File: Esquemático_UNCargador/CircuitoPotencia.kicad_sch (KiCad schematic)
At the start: 0 parts

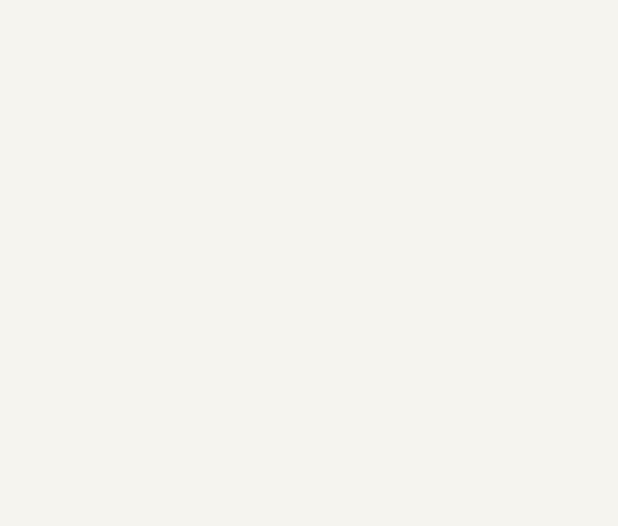
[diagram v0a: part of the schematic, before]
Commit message: Se modifica esquema del micro y se agrega página de sensores
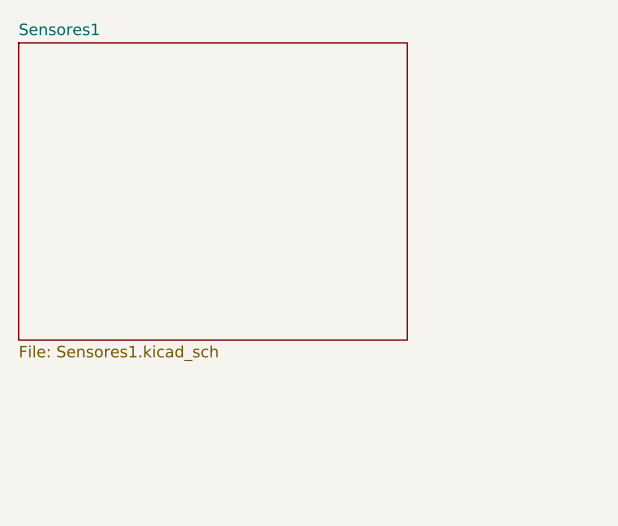
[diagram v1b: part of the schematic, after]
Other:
- added sheet Sensores1 (Sensores1.kicad_sch)
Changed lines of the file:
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@@
+    )
+  )
+  (sheet (at 55.88 40.64) (size 43.18 33.02) (fields_autoplaced)
+    (stroke (width 0.1524) (type solid))
+    (fill (color 0 0 0 0.0000))
+    (property "Sheetname" "Sensores1" (at 55.88 39.9284 0)
+      (effects (font (size 1.27 1.27)) (justify left bottom))
+    )
+    (property "Sheetfile" "Sensores1.kicad_sch" (at 55.88 74.2446 0)
+      (effects (font (size 1.27 1.27)) (justify left top))
+    )
+    (instances
+      (project "CircuitoPotencia"
+        (path "/f64e4c48-29c2-4644-b6e3-d55b9152fc29" (page "5"))
+      )
     )
   )

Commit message: Pinout sensores
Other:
- sheet Microcontrolador ports: added FALLA, GFCI_TEST, NTC_Analog, RX_01, TX_01; removed none
- sheet Sensores1 ports: added FALLA, GFCI_TEST, NTC_Analog, RX_01, TX_01; removed none
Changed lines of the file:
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@@
 (kicad_sch (version 20230121) (generator eeschema)
   (paper "A4")
+  (wire (pts (xy 89.3064 73.66) (xy 89.3064 118.11))
+    (stroke (width 0) (type default))
+  )
+  (wire (pts (xy 67.564 73.66) (xy 67.564 118.11))
+    (stroke (width 0) (type default))
+  )
+  (wire (pts (xy 79.9592 73.66) (xy 79.9592 118.11))
+    (stroke (width 0) (type default))
+  )
+  (wire (pts (xy 83.7692 73.66) (xy 83.7692 118.11))
+    (stroke (width 0) (type default))
+  )
   (wire (pts (xy 96.52 134.62) (xy 133.35 134.62))
+    (stroke (width 0) (type default))
+  )
+  (wire (pts (xy 83.7692 73.66) (xy 83.7184 73.66))
+    (stroke (width 0) (type default))
+  )
+  (wire (pts (xy 73.8124 73.66) (xy 73.8124 118.11))
+    (stroke (width 0) (type default))
+  )
+  (wire (pts (xy 79.9592 118.11) (xy 79.9084 118.11))
     (stroke (width 0) (type default))
   )
@@
     )
     (pin "pilot_PWM" output (at 96.52 134.62 0)
+      (effects (font (size 1.27 1.27)) (justify right))
+    )
+    (pin "GFCI_TEST" input (at 89.3064 118.11 90)
+      (effects (font (size 1.27 1.27)) (justify right))
+    )
+    (pin "FALLA" input (at 67.564 118.11 90)
+      (effects (font (size 1.27 1.27)) (justify right))
+    )
+    (pin "NTC_Analog" input (at 73.8124 118.11 90)
+      (effects (font (size 1.27 1.27)) (justify right))
+    )
+    (pin "RX_01" input (at 79.9084 118.11 90)
+      (effects (font (size 1.27 1.27)) (justify right))
+    )
+    (pin "TX_01" input (at 83.7692 118.11 90)
       (effects (font (size 1.27 1.27)) (justify right))
     )
@@
       (effects (font (size 1.27 1.27)) (justify left top))
     )
+    (pin "FALLA" input (at 67.564 73.66 270)
+      (effects (font (size 1.27 1.27)) (justify left))
+    )
+    (pin "RX_01" input (at 79.9592 73.66 270)
+      (effects (font (size 1.27 1.27)) (justify left))
+    )
+    (pin "GFCI_TEST" input (at 89.3064 73.66 270)
+      (effects (font (size 1.27 1.27)) (justify left))
+    )
+    (pin "TX_01" input (at 83.7184 73.66 270)
+      (effects (font (size 1.27 1.27)) (justify left))
+    )
+    (pin "NTC_Analog" input (at 73.8124 73.66 270)
+      (effects (font (size 1.27 1.27)) (justify left))
+    )
     (instances

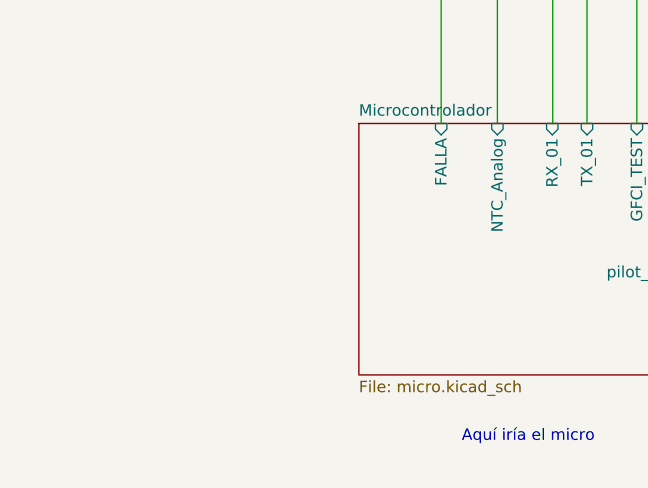
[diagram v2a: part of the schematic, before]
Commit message: Avances en Huellas
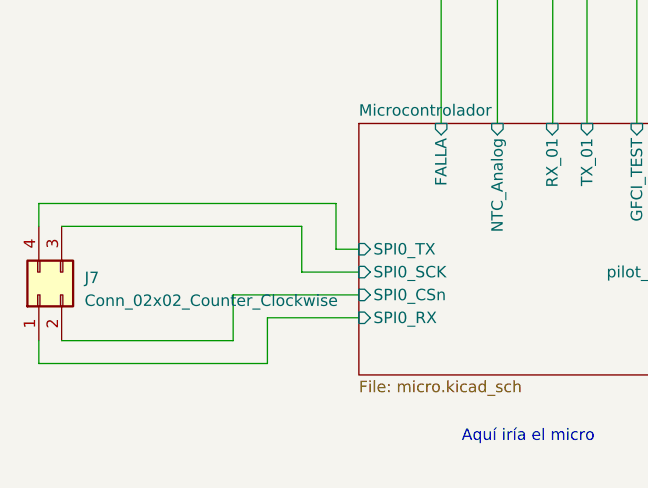
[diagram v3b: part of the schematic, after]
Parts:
- added J7: Conn_02x02_Counter_Clockwise, Connector_PinHeader_2.54mm:PinHeader_2x02_P2.54mm_Vertical, symbol Connector_Generic:Conn_02x02_Counter_Clockwise
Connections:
- new net Microcontrolador/SPI0_CSn: J7.2 (Pin_2)
- new net Microcontrolador/SPI0_RX: J7.1 (Pin_1)
- new net Microcontrolador/SPI0_SCK: J7.3 (Pin_3)
- new net Microcontrolador/SPI0_TX: J7.4 (Pin_4)
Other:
- sheet Microcontrolador ports: added SPI0_CSn, SPI0_RX, SPI0_SCK, SPI0_TX; removed none
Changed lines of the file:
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@@
 (kicad_sch (version 20230121) (generator eeschema)
   (paper "A4")
+  (wire (pts (xy 48.26 139.7) (xy 58.42 139.7))
+    (stroke (width 0) (type default))
+  )
+  (wire (pts (xy 52.07 134.62) (xy 52.07 129.54))
+    (stroke (width 0) (type default))
+  )
+  (wire (pts (xy 44.45 142.24) (xy 44.45 137.16))
+    (stroke (width 0) (type default))
+  )
   (wire (pts (xy 89.3064 73.66) (xy 89.3064 118.11))
+    (stroke (width 0) (type default))
+  )
+  (wire (pts (xy 58.42 134.62) (xy 52.07 134.62))
+    (stroke (width 0) (type default))
+  )
+  (wire (pts (xy 22.86 129.54) (xy 22.86 127))
+    (stroke (width 0) (type default))
+  )
+  (wire (pts (xy 55.88 127) (xy 55.88 132.08))
     (stroke (width 0) (type default))
   )
@@
     (stroke (width 0) (type default))
   )
+  (wire (pts (xy 52.07 129.54) (xy 25.4 129.54))
+    (stroke (width 0) (type default))
+  )
+  (wire (pts (xy 22.86 142.24) (xy 22.86 144.78))
+    (stroke (width 0) (type default))
+  )
   (wire (pts (xy 96.52 134.62) (xy 133.35 134.62))
+    (stroke (width 0) (type default))
+  )
+  (wire (pts (xy 44.45 137.16) (xy 58.42 137.16))
+    (stroke (width 0) (type default))
+  )
+  (wire (pts (xy 25.4 142.24) (xy 44.45 142.24))
     (stroke (width 0) (type default))
   )
@@
   )
   (wire (pts (xy 79.9592 118.11) (xy 79.9084 118.11))
+    (stroke (width 0) (type default))
+  )
+  (wire (pts (xy 22.86 144.78) (xy 48.26 144.78))
+    (stroke (width 0) (type default))
+  )
+  (wire (pts (xy 55.88 132.08) (xy 58.42 132.08))
+    (stroke (width 0) (type default))
+  )
+  (wire (pts (xy 22.86 127) (xy 55.88 127))
+    (stroke (width 0) (type default))
+  )
+  (wire (pts (xy 48.26 144.78) (xy 48.26 139.7))
     (stroke (width 0) (type default))
   )
@@
     (at 142.24 82.55 0)
     (effects (font (size 1.27 1.27)) (justify left bottom))
+  )
+  (symbol (lib_id "Connector_Generic:Conn_02x02_Counter_Clockwise") (at 22.86 137.16 90) (unit 1)
+    (in_bom yes) (on_board yes) (dnp no) (fields_autoplaced)
+    (property "Reference" "J7" (at 27.94 135.255 90)
+      (effects (font (size 1.27 1.27)) (justify right))
+    )
+    (property "Value" "Conn_02x02_Counter_Clockwise" (at 27.94 137.795 90)
+      (effects (font (size 1.27 1.27)) (justify right))
+    )
+    (property "Footprint" "Connector_PinHeader_2.54mm:PinHeader_2x02_P2.54mm_Vertical" (at 22.86 137.16 0)
+      (effects (font (size 1.27 1.27)) hide)
+    )
+    (property "Datasheet" "~" (at 22.86 137.16 0)
+      (effects (font (size 1.27 1.27)) hide)
+    )
+    (pin "1")
+    (pin "2")
+    (pin "3")
+    (pin "4")
+    (instances
+      (project "CircuitoPotencia"
+        (path "/f64e4c48-29c2-4644-b6e3-d55b9152fc29"
+          (reference "J7") (unit 1)
+        )
+      )
+    )
   )
   (sheet (at 58.42 118.11) (size 38.1 27.94) (fields_autoplaced)
@@
       (effects (font (size 1.27 1.27)) (justify right))
     )
+    (pin "SPI0_TX" input (at 58.42 132.08 180)
+      (effects (font (size 1.27 1.27)) (justify left))
+    )
+    (pin "SPI0_SCK" input (at 58.42 134.62 180)
+      (effects (font (size 1.27 1.27)) (justify left))
+    )
+    (pin "SPI0_CSn" input (at 58.42 137.16 180)
+      (effects (font (size 1.27 1.27)) (justify left))
+    )
+    (pin "SPI0_RX" input (at 58.42 139.7 180)
+      (effects (font (size 1.27 1.27)) (justify left))
+    )
     (instances

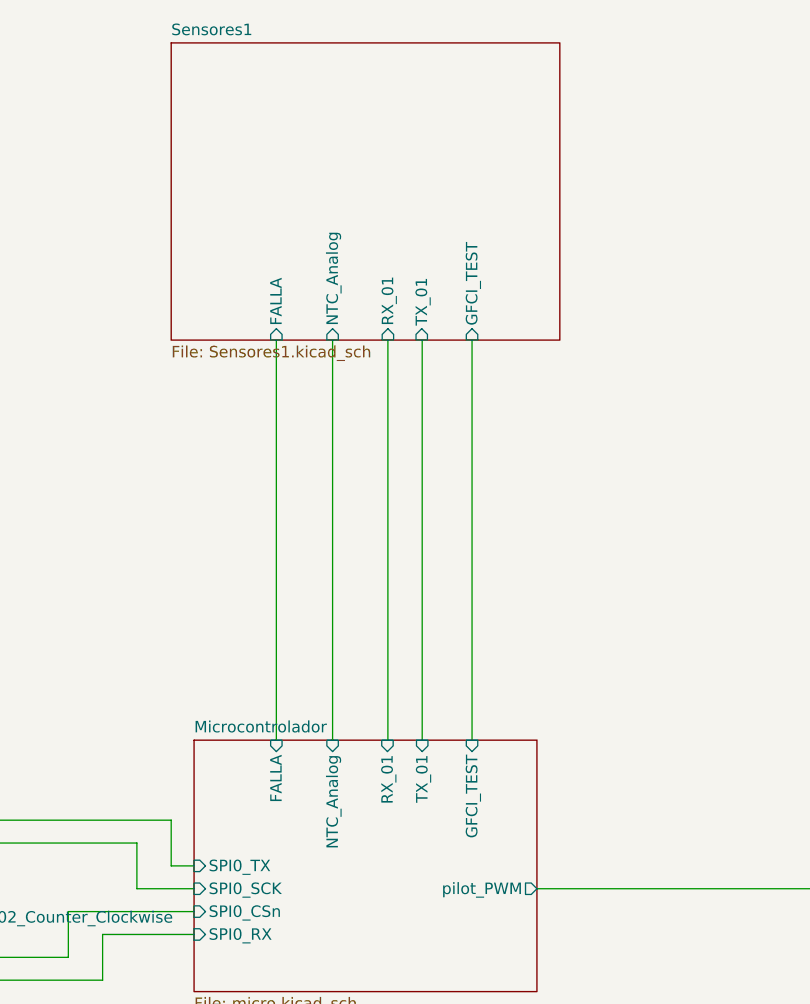
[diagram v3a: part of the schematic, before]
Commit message: Modificación de la huella del microcontrolador
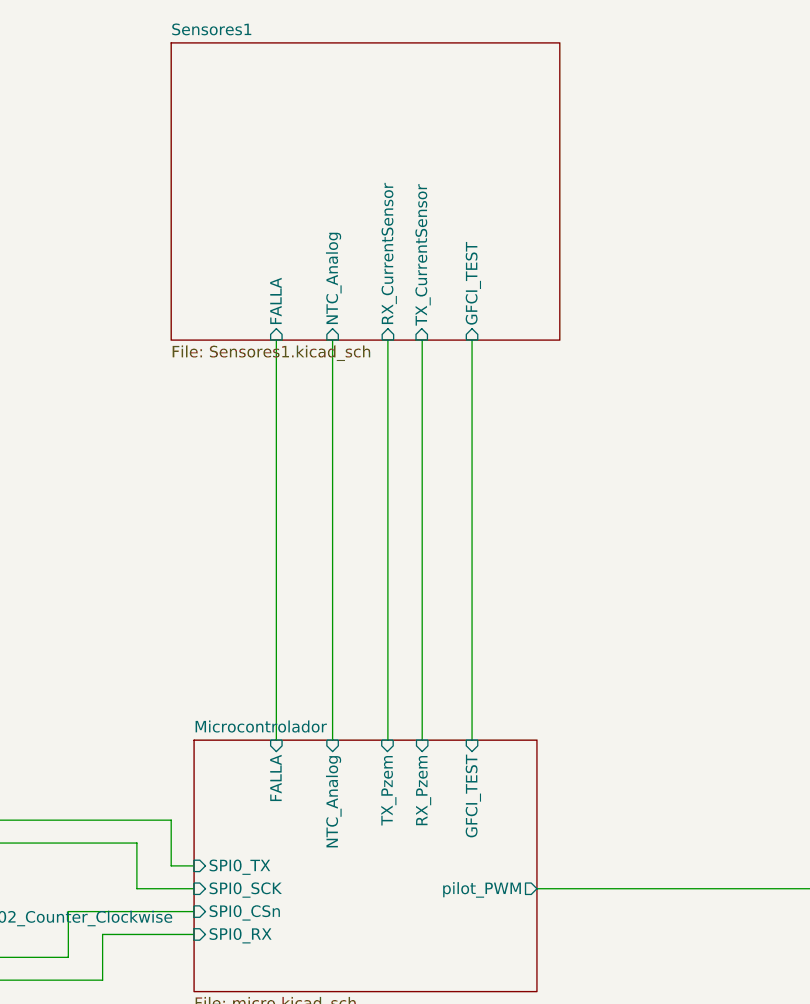
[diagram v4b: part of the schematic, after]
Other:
- sheet Microcontrolador ports: added RX_Pzem, TX_Pzem; removed RX_01, TX_01
- sheet Sensores1 ports: added RX_CurrentSensor, TX_CurrentSensor; removed RX_01, TX_01
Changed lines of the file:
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@@
       (effects (font (size 1.27 1.27)) (justify right))
     )
-    (pin "RX_01" input (at 79.9084 118.11 90)
+    (pin "TX_Pzem" input (at 79.9084 118.11 90)
       (effects (font (size 1.27 1.27)) (justify right))
     )
-    (pin "TX_01" input (at 83.7692 118.11 90)
+    (pin "RX_Pzem" input (at 83.7692 118.11 90)
       (effects (font (size 1.27 1.27)) (justify right))
     )
@@
       (effects (font (size 1.27 1.27)) (justify left))
     )
-    (pin "RX_01" input (at 79.9592 73.66 270)
+    (pin "RX_CurrentSensor" input (at 79.9592 73.66 270)
       (effects (font (size 1.27 1.27)) (justify left))
     )
@@
       (effects (font (size 1.27 1.27)) (justify left))
     )
-    (pin "TX_01" input (at 83.7184 73.66 270)
+    (pin "TX_CurrentSensor" input (at 83.7184 73.66 270)
       (effects (font (size 1.27 1.27)) (justify left))
     )

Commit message: Cambios de recomendaciones profesor
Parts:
- removed J7: Conn_02x02_Counter_Clockwise, Connector_PinHeader_2.54mm:PinHeader_2x02_P2.54mm_Vertical, symbol Connector_Generic:Conn_02x02_Counter_Clockwise
- added J2: InV, Connector_Molex:Molex_KK-254_AE-6410-02A_1x02_P2.54mm_Vertical, symbol Connector:Conn_01x02_Socket
- added J3: Conn_02x03_Counter_Clockwise, Connector_PinHeader_2.54mm:PinHeader_2x03_P2.54mm_Vertical, symbol Connector_Generic:Conn_02x03_Counter_Clockwise
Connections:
- net Microcontrolador/SPI0_CSn: now also J3.3 (Pin_3)
- net Microcontrolador/SPI0_RX: now also J3.2 (Pin_2)
- net Microcontrolador/SPI0_SCK: now also J3.4 (Pin_4)
- net Microcontrolador/SPI0_TX: now also J3.5 (Pin_5)
- new net GND: J3.1 (Pin_1)
- new net Potencia2.0/In110v: J2.1 (Pin_1)
- new net Potencia2.0/N: J2.2 (Pin_2)
- no-connect marks 0 -> 1
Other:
- sheet Potencia2.0 ports: added In110v, N; removed none
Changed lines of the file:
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@@
 (kicad_sch (version 20230121) (generator eeschema)
   (paper "A4")
+  (no_connect (at 20.32 129.54))
   (wire (pts (xy 48.26 139.7) (xy 58.42 139.7))
     (stroke (width 0) (type default))
@@
     (stroke (width 0) (type default))
   )
+  (wire (pts (xy 185.42 57.15) (xy 181.61 57.15))
+    (stroke (width 0) (type default))
+  )
   (wire (pts (xy 83.7692 73.66) (xy 83.7692 118.11))
     (stroke (width 0) (type default))
@@
     (stroke (width 0) (type default))
   )
+  (wire (pts (xy 189.23 55.88) (xy 185.42 55.88))
+    (stroke (width 0) (type default))
+  )
+  (wire (pts (xy 185.42 53.34) (xy 185.42 52.07))
+    (stroke (width 0) (type default))
+  )
   (wire (pts (xy 22.86 142.24) (xy 22.86 144.78))
     (stroke (width 0) (type default))
   )
+  (wire (pts (xy 189.23 53.34) (xy 185.42 53.34))
+    (stroke (width 0) (type default))
+  )
   (wire (pts (xy 96.52 134.62) (xy 133.35 134.62))
     (stroke (width 0) (type default))
@@
     (stroke (width 0) (type default))
   )
+  (wire (pts (xy 20.32 142.24) (xy 20.32 146.05))
+    (stroke (width 0) (type default))
+  )
   (wire (pts (xy 25.4 142.24) (xy 44.45 142.24))
     (stroke (width 0) (type default))
   )
   (wire (pts (xy 83.7692 73.66) (xy 83.7184 73.66))
+    (stroke (width 0) (type default))
+  )
+  (wire (pts (xy 185.42 52.07) (xy 181.61 52.07))
+    (stroke (width 0) (type default))
+  )
+  (wire (pts (xy 185.42 55.88) (xy 185.42 57.15))
     (stroke (width 0) (type default))
   )
@@
     (effects (font (size 1.27 1.27)) (justify left bottom))
   )
-  (symbol (lib_id "Connector_Generic:Conn_02x02_Counter_Clockwise") (at 22.86 137.16 90) (unit 1)
+  (symbol (lib_id "power:GND") (at 20.32 146.05 0) (unit 1)
     (in_bom yes) (on_board yes) (dnp no) (fields_autoplaced)
-    (property "Reference" "J7" (at 27.94 135.255 90)
-      (effects (font (size 1.27 1.27)) (justify right))
-    )
-    (property "Value" "Conn_02x02_Counter_Clockwise" (at 27.94 137.795 90)
-      (effects (font (size 1.27 1.27)) (justify right))
-    )
-    (property "Footprint" "Connector_PinHeader_2.54mm:PinHeader_2x02_P2.54mm_Vertical" (at 22.86 137.16 0)
+    (property "Reference" "#PWR011" (at 20.32 152.4 0)
+      (effects (font (size 1.27 1.27)) hide)
+    )
+    (property "Value" "GND" (at 20.32 151.13 0)
+      (effects (font (size 1.27 1.27)))
+    )
+    (property "Footprint" "" (at 20.32 146.05 0)
+      (effects (font (size 1.27 1.27)) hide)
+    )
+    (property "Datasheet" "" (at 20.32 146.05 0)
+      (effects (font (size 1.27 1.27)) hide)
+    )
+    (pin "1")
+    (instances
+      (project "CircuitoPotencia"
+        (path "/f64e4c48-29c2-4644-b6e3-d55b9152fc29"
+          (reference "#PWR011") (unit 1)
+        )
+      )
+    )
+  )
+  (symbol (lib_id "Connector:Conn_01x02_Socket") (at 194.31 53.34 0) (unit 1)
+    (in_bom yes) (on_board yes) (dnp no) (fields_autoplaced)
+    (property "Reference" "J2" (at 195.58 53.975 0)
+      (effects (font (size 1.27 1.27)) (justify left))
+    )
+    (property "Value" "InV" (at 195.58 56.515 0)
+      (effects (font (size 1.27 1.27)) (justify left))
+    )
+    (property "Footprint" "Connector_Molex:Molex_KK-254_AE-6410-02A_1x02_P2.54mm_Vertical" (at 194.31 53.34 0)
+      (effects (font (size 1.27 1.27)) hide)
+    )
+    (property "Datasheet" "~" (at 194.31 53.34 0)
+      (effects (font (size 1.27 1.27)) hide)
+    )
+    (pin "1")
+    (pin "2")
+    (instances
+      (project "CircuitoPotencia"
+        (path "/f64e4c48-29c2-4644-b6e3-d55b9152fc29/27c27843-11c4-470f-a3f9-e81d775d20fc"
+          (reference "J2") (unit 1)
+        )
+        (path "/f64e4c48-29c2-4644-b6e3-d55b9152fc29"
+          (reference "J7") (unit 1)
+        )
+      )
+    )
+  )
+  (symbol (lib_id "Connector_Generic:Conn_02x03_Counter_Clockwise") (at 22.86 137.16 90) (unit 1)
+    (in_bom yes) (on_board yes) (dnp no) (fields_autoplaced)
+    (property "Reference" "J3" (at 27.94 135.255 90)
+      (effects (font (size 1.27 1.27)) (justify right))
+    )
+    (property "Value" "Conn_02x03_Counter_Clockwise" (at 27.94 137.795 90)
+      (effects (font (size 1.27 1.27)) (justify right))
+    )
+    (property "Footprint" "Connector_PinHeader_2.54mm:PinHeader_2x03_P2.54mm_Vertical" (at 22.86 137.16 0)
       (effects (font (size 1.27 1.27)) hide)
     )
@@
     (pin "3")
     (pin "4")
+    (pin "5")
+    (pin "6")
     (instances
       (project "CircuitoPotencia"
         (path "/f64e4c48-29c2-4644-b6e3-d55b9152fc29"
-          (reference "J7") (unit 1)
+          (reference "J3") (unit 1)
         )
       )
@@
       (effects (font (size 1.27 1.27)) (justify left top))
     )
-    (instances
+    (pin "In110v" input (at 181.61 52.07 0)
+      (effects (font (size 1.27 1.27)) (justify right))
+    )
+    (pin "N" input (at 181.61 57.15 0)
+      (effects (font (size 1.27 1.27)) (justify right))
+    )
+    (instances

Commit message: Actualización17.0
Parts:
- J2: value InV -> Neutro; footprint Connector_Molex:Molex_KK-254_AE-6410-02A_1x02_P2.54mm_Vertical -> TerminalBlock:TerminalBlock_Wuerth_691311400102_P7.62mm
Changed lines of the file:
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@@
       (effects (font (size 1.27 1.27)) (justify left))
     )
-    (property "Value" "InV" (at 195.58 56.515 0)
+    (property "Value" "Neutro" (at 195.58 56.515 0)
       (effects (font (size 1.27 1.27)) (justify left))
     )
-    (property "Footprint" "Connector_Molex:Molex_KK-254_AE-6410-02A_1x02_P2.54mm_Vertical" (at 194.31 53.34 0)
+    (property "Footprint" "TerminalBlock:TerminalBlock_Wuerth_691311400102_P7.62mm" (at 194.31 53.34 0)
       (effects (font (size 1.27 1.27)) hide)
     )
@@
         )
         (path "/f64e4c48-29c2-4644-b6e3-d55b9152fc29"
-          (reference "J7") (unit 1)
+          (reference "Input110") (unit 1)
         )
       )
